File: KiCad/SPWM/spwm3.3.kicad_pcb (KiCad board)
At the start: 2 copper layers, 70 x 20 mm, 16 parts, among them U1 SMARTPWM V3, U4 24G PAD, U5 24G PAD, U6 24G PAD, U7 24G PAD

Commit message: Update silkscreen, Generate new Gerbers
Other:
- board text added: "JLCJLCJLCJLC"
- board text added: "S1"
- board text added: "Smart PWM V3(Rev C) ATI DNA250C Style PCB"
- board text removed: "S3"
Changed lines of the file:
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@@
   (general
     (thickness 1.6)
-    (drawings 37)
+    (drawings 39)
     (tracks 99)
     (zones 0)
@@
       (net 4 GND) (solder_mask_margin 0.1016) (zone_connect 2))
   )
+  (gr_text JLCJLCJLCJLC (at 137.07 113.15) (layer F.SilkS)
+    (effects (font (size 1 0.703) (thickness 0.17575)) (justify left top))
+  )
+  (gr_text "Smart PWM V3(Rev C)\nATI DNA250C Style PCB" (at 167.97 96.2) (layer B.SilkS)
+    (effects (font (size 0.703 0.703) (thickness 0.17575)) (justify left top mirror))
+  )
   (gr_arc (start 182.101272 113.603772) (end 182.1011 115.0036) (angle -90.014114) (layer Edge.Cuts) (width 0.15))
   (gr_line (start 183.5011 113.6036) (end 183.5011 111.1536) (layer Edge.Cuts) (width 0.15))
@@
   (gr_line (start 113.0291 105.0036) (end 185.7791 105.0036) (layer F.Fab) (width 0.15))
   (gr_line (start 170.5971 107.0036) (end 170.5971 103.0036) (layer F.Fab) (width 0.15))
-  (gr_text S2 (at 156.7131 108.9276) (layer F.SilkS)
-    (effects (font (size 0.703 0.703) (thickness 0.0814)) (justify left top))
-  )
-  (gr_text S3 (at 163.2631 108.9276) (layer F.SilkS)
-    (effects (font (size 0.703 0.703) (thickness 0.0814)) (justify left top))
+  (gr_text S1 (at 156.7131 108.9276) (layer F.SilkS)
+    (effects (font (size 0.703 0.703) (thickness 0.17575)) (justify left top))
+  )
+  (gr_text S2 (at 163.2631 108.9276) (layer F.SilkS)
+    (effects (font (size 0.703 0.703) (thickness 0.17575)) (justify left top))
   )
   (gr_text S4 (at 174.9631 110.3776) (layer F.SilkS)
-    (effects (font (size 0.703 0.703) (thickness 0.0814)) (justify left top))
+    (effects (font (size 0.703 0.703) (thickness 0.17575)) (justify left top))
   )
   (gr_text R1 (at 169.9131 109.6276) (layer F.SilkS)
-    (effects (font (size 0.703 0.703) (thickness 0.0814)) (justify left top))
+    (effects (font (size 0.703 0.703) (thickness 0.17575)) (justify left top))
   )
   (gr_text U (at 157.1131 99.9276) (layer F.SilkS)
-    (effects (font (size 0.703 0.703) (thickness 0.0814)) (justify left top))
+    (effects (font (size 0.703 0.703) (thickness 0.17575)) (justify left top))
   )
   (gr_text D (at 163.6631 99.9276) (layer F.SilkS)
-    (effects (font (size 0.703 0.703) (thickness 0.0814)) (justify left top))
+    (effects (font (size 0.703 0.703) (thickness 0.17575)) (justify left top))
   )
   (gr_text D1 (at 170.0131 101.2776) (layer F.SilkS)
-    (effects (font (size 0.703 0.703) (thickness 0.0814)) (justify left top))
+    (effects (font (size 0.703 0.703) (thickness 0.17575)) (justify left top))
   )
   (gr_text ON (at 174.9631 98.4776) (layer F.SilkS)
-    (effects (font (size 0.703 0.703) (thickness 0.0814)) (justify left top))
+    (effects (font (size 0.703 0.703) (thickness 0.17575)) (justify left top))
   )
   (gr_text B (at 182.15 97.66) (layer B.SilkS)
@@
     (effects (font (size 1 1) (thickness 0.25)) (justify right top mirror))
   )
-  (gr_text V (at 156.95 107.91) (layer B.SilkS)
+  (gr_text V (at 160.41 107.68) (layer B.SilkS)
     (effects (font (size 1 1) (thickness 0.25)) (justify right top mirror))
   )
-  (gr_text M (at 156.81 109.33) (layer B.SilkS)
+  (gr_text M (at 160.27 109.1) (layer B.SilkS)
     (effects (font (size 1 1) (thickness 0.25)) (justify right top mirror))
   )
-  (gr_text M (at 156.81 110.96) (layer B.SilkS)
+  (gr_text M (at 160.27 110.72) (layer B.SilkS)
     (effects (font (size 1 1) (thickness 0.25)) (justify right top mirror))
   )
-  (gr_text V (at 154.63 107.91) (layer B.SilkS)
+  (gr_text V (at 157.34 107.68) (layer B.SilkS)
     (effects (font (size 1 1) (thickness 0.25)) (justify right top mirror))
   )
-  (gr_text M (at 154.49 109.33) (layer B.SilkS)
+  (gr_text M (at 157.2 109.1) (layer B.SilkS)
     (effects (font (size 1 1) (thickness 0.25)) (justify right top mirror))
   )
-  (gr_text + (at 154.19 110.58) (layer B.SilkS)
+  (gr_text + (at 156.9 110.34) (layer B.SilkS)
     (effects (font (size 1.406 1.406) (thickness 0.25)) (justify right top mirror))
   )
-  (gr_text V (at 152.36 107.91) (layer B.SilkS)
+  (gr_text V (at 154.24 107.68) (layer B.SilkS)
     (effects (font (size 1 1) (thickness 0.25)) (justify right top mirror))
   )
-  (gr_text M (at 152.22 109.33) (layer B.SilkS)
+  (gr_text M (at 154.1 109.1) (layer B.SilkS)
     (effects (font (size 1 1) (thickness 0.25)) (justify right top mirror))
   )
-  (gr_text - (at 151.92 110.575) (layer B.SilkS)
+  (gr_text - (at 153.8 110.345) (layer B.SilkS)
     (effects (font (size 1.406 1.406) (thickness 0.25)) (justify right top mirror))
   )

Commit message: Update all the things
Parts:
- added S1: Fire, spwm3.3:KSC641JLFS, F.Cu at (117.5, 105.0)
- moved Pad4 1.00 mm to (122.5, 102.1)
- moved Pad7 1.00 mm to (122.4, 107.9)
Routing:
- net FIRE_SW: track 67.6 -> 82.9 mm
- net GND: track 83.7 -> 91.9 mm
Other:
- board text added: "F"
- board text added: "S3"
- board text added: "SmartPWM v3 (Rev C) MosMax Electronics"
- board text removed: "Smart PWM V3(Rev C) ATI DNA250C Style PCB"

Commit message: Cleanup and make pretty rendering
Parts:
- added VM: VM, spwm3.3:VM, F.Cu at (140.7, 105.1)
- D1: footprint vm-moved:SSL-LX40FT3ID -> spwm3.3:SSL-LX40FT3ID
- Pad1, Pad3, Pad5, Pad6: footprint vm-moved:Pad -> spwm3.3:Pad
- Pad4: footprint vm-moved:Pad_Pad4 -> spwm3.3:Pad_Pad4
- Pad7: footprint vm-moved:Pad_Pad7 -> spwm3.3:Pad_Pad7
- R1: footprint vm-moved:RES_0805edit -> spwm3.3:RES_0805edit
- S2, S3: footprint vm-moved:KSC641JLFS -> spwm3.3:KSC641JLFS
- S4: footprint vm-moved:SS-12D07-VG4NSGAPA -> spwm3.3:SS-12D07-VG4NSGAPA
- U1: footprint vm-moved:SmartPWM_V3 -> spwm3.3:SmartPWM_V3
- U4: footprint vm-moved:24g_pad_U4 -> spwm3.3:24g_pad_U4
- U5, U6, U7: footprint vm-moved:24g_pad_U5 -> spwm3.3:24g_pad_U5

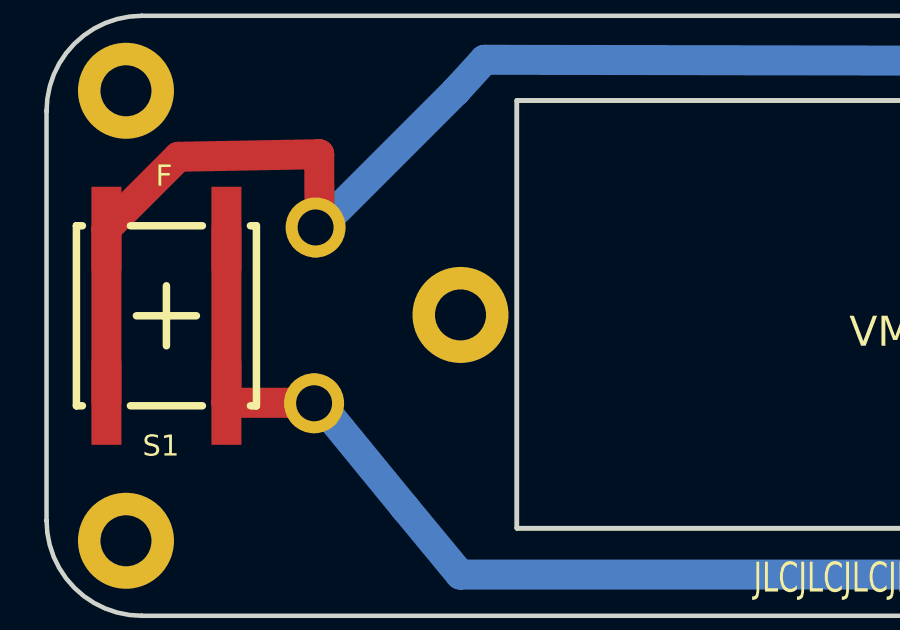
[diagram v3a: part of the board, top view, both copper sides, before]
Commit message: Cleanup SPWM, Upload from scratch written project with proper schematic
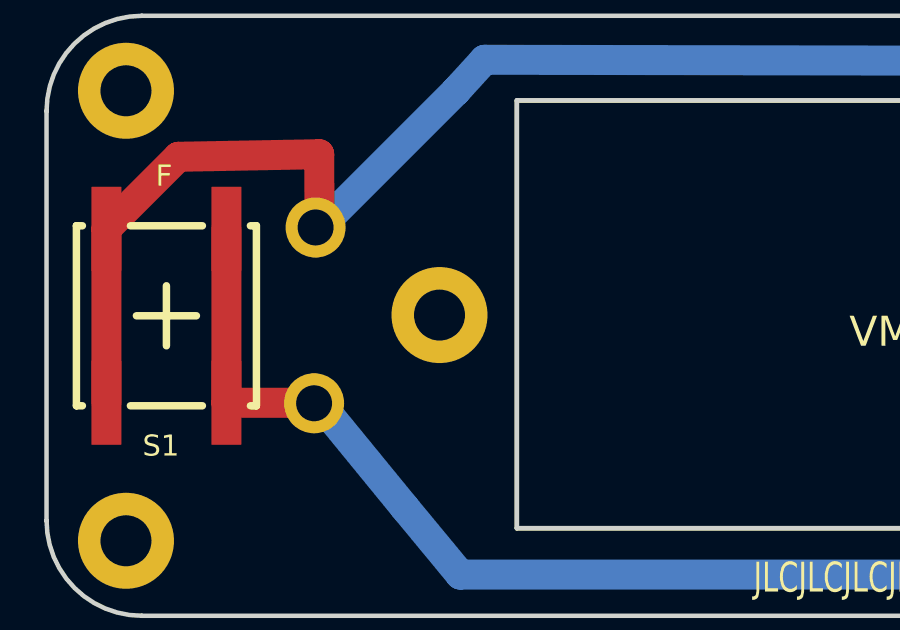
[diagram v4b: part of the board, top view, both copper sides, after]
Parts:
- moved Pad1 0.70 mm to (126.6, 105.0)
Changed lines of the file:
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@@
-(kicad_pcb (version 20171130) (host pcbnew 5.1.0-unknown-9bfce26~82~ubuntu18.04.1)
+(kicad_pcb (version 20171130) (host pcbnew 5.1.0-unknown-7e34a5a~82~ubuntu18.04.1)
   (general
     (thickness 1.6)
@@
   )
   (module spwm3.3:Pad (layer Top)
-    (at 127.3 104.975 90)
+    (at 126.6 104.98 90)
     (fp_text reference Pad1 (at 0 0 90) (layer F.SilkS) hide
       (effects (font (size 1.27 1.27) (thickness 0.15)))
